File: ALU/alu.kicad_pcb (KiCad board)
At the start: 2 copper layers, 90.2 x 88.9 mm, 70 parts, among them J1 Bus, J2 Power, J3 Misc, J4 A Register, J5 B Register, U1 74LS08, U2 74LS173, U3 74LS02, U4 74LS245, U5 74LS283, U6 74LS283, U7 74LS86, U8 74LS86

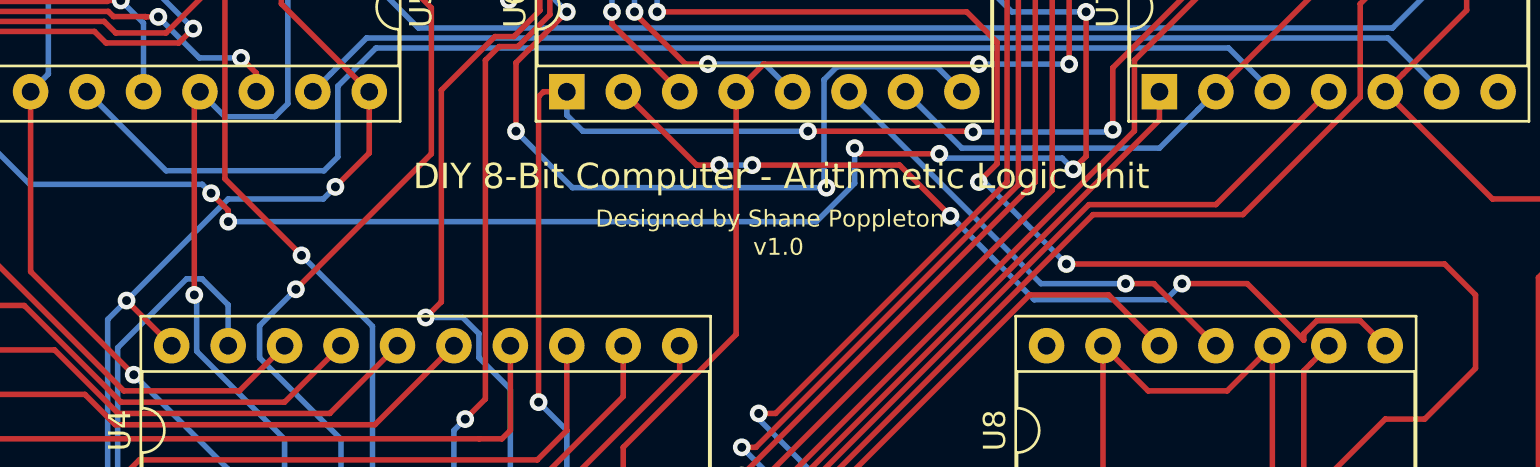
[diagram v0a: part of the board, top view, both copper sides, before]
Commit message: Clock: Added attributions, re-plotted gerbers
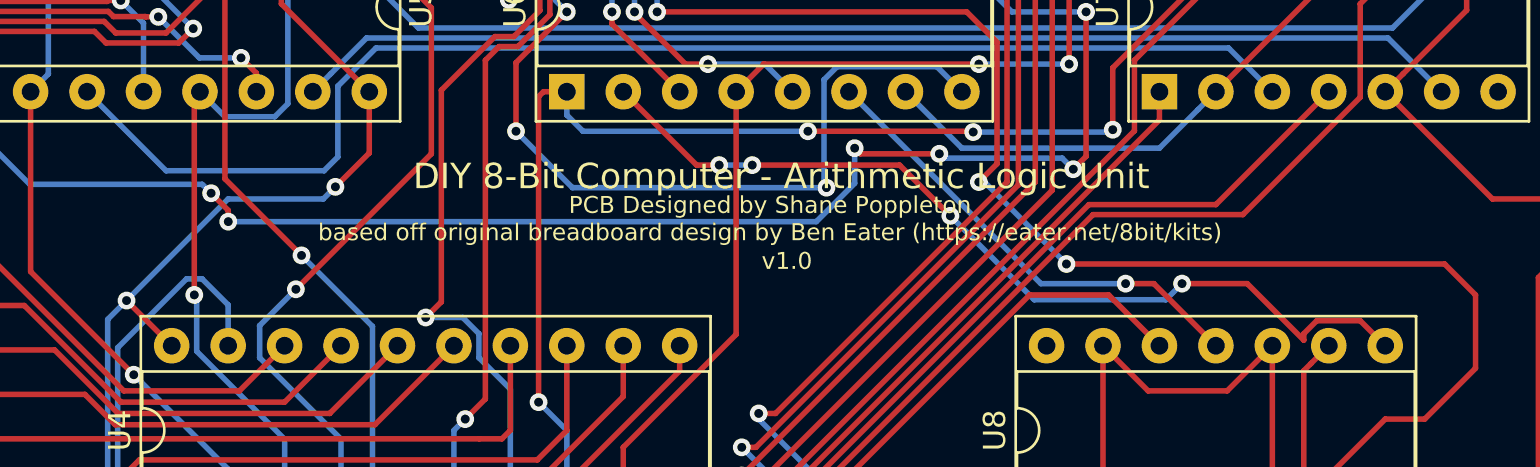
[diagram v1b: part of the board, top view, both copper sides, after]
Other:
- board text added: "PCB Designed by Shane Poppleton based off original breadboard design by Ben Eater (https://eater.net/8bit/kits)"
- board text removed: "Designed by Shane Poppleton"
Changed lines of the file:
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@@
     )
   )
-  (gr_text v1.0 (at 73.025 93.345) (layer F.SilkS)
+  (gr_text v1.0 (at 73.406 93.98) (layer F.SilkS)
     (effects (font (size 0.762 0.762) (thickness 0.127)))
   )
-  (gr_text "Designed by Shane Poppleton" (at 72.644 92.075) (layer F.SilkS)
+  (gr_text "PCB Designed by Shane Poppleton\nbased off original breadboard design by Ben Eater (https://eater.net/8bit/kits)" (at 72.644 92.075) (layer F.SilkS)
     (effects (font (size 0.762 0.762) (thickness 0.127)))
   )

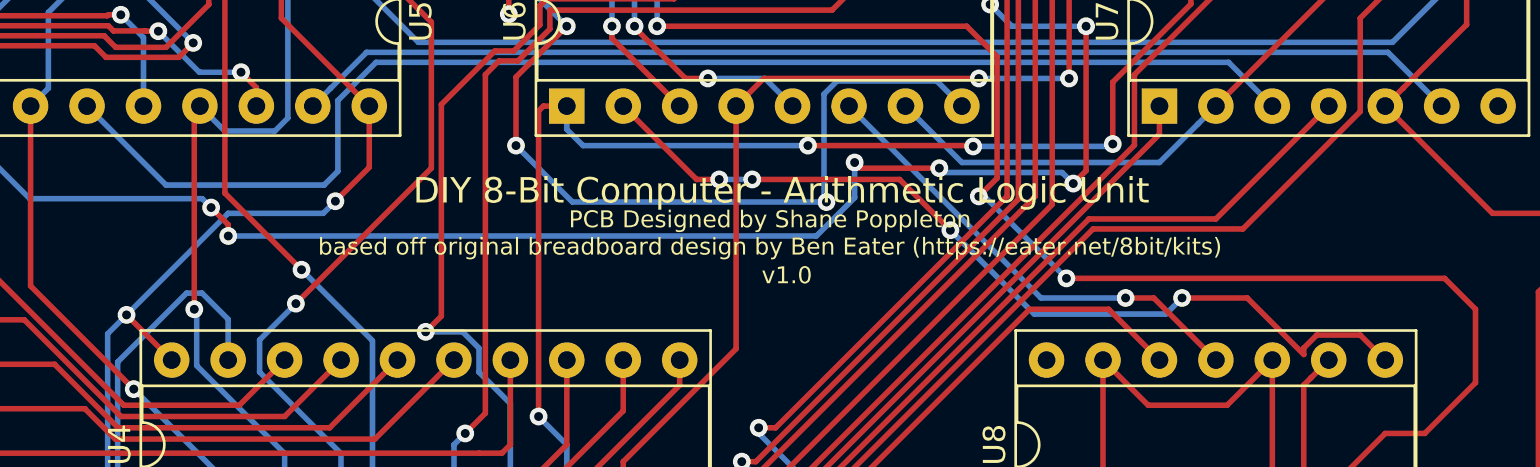
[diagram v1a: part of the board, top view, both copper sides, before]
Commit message: Added Attribution on each PCB, and regenerated gerbers
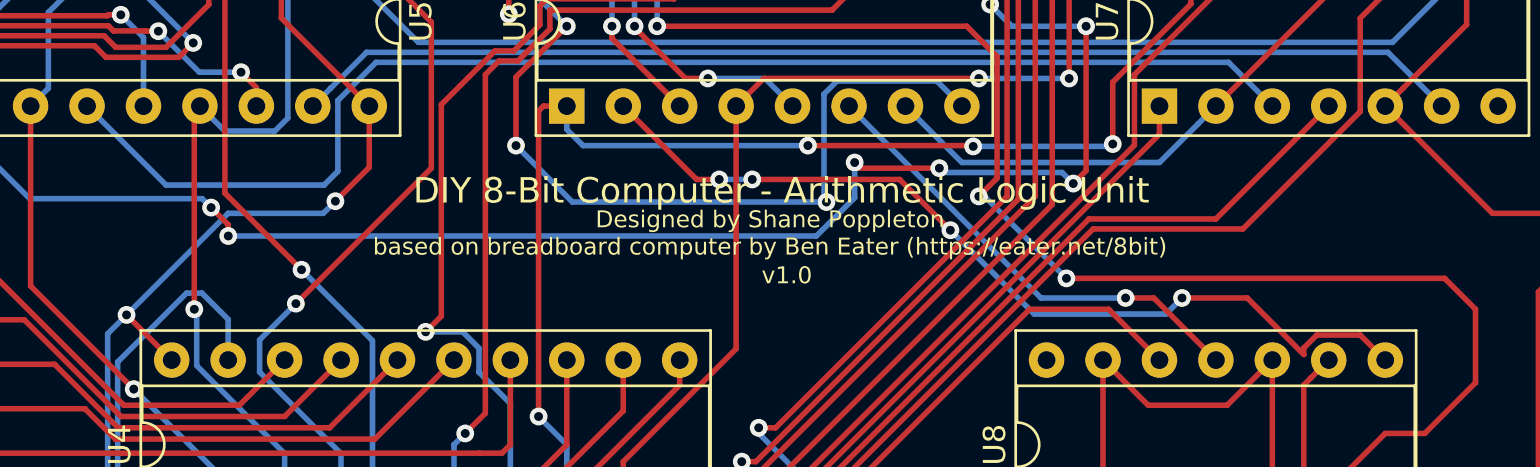
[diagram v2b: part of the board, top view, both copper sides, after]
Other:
- board text added: "Designed by Shane Poppleton based on breadboard computer by Ben Eater (https://eater.net/8bit)"
- board text removed: "PCB Designed by Shane Poppleton based off original breadboard design by Ben Eater (https://eater.net/8bit/kits)"
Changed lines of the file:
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@@
     (effects (font (size 0.762 0.762) (thickness 0.127)))
   )
-  (gr_text "PCB Designed by Shane Poppleton\nbased off original breadboard design by Ben Eater (https://eater.net/8bit/kits)" (at 72.644 92.075) (layer F.SilkS)
+  (gr_text "Designed by Shane Poppleton\nbased on breadboard computer by Ben Eater (https://eater.net/8bit)\n" (at 72.644 92.075) (layer F.SilkS)
     (effects (font (size 0.762 0.762) (thickness 0.127)))
   )
